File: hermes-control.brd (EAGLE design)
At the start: 106 x 47 mm, 73 parts, among them J1 1981568-1, J3 2201778-1, Q2 BC849SMD, Q3 FDN360P, Q4 FDN360P, Q5 BC849SMD, Q6 MMBT3906SOT23-3, Q7 FDN360P, Q8 MMBT2222A, U1 LSM9DS1TR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

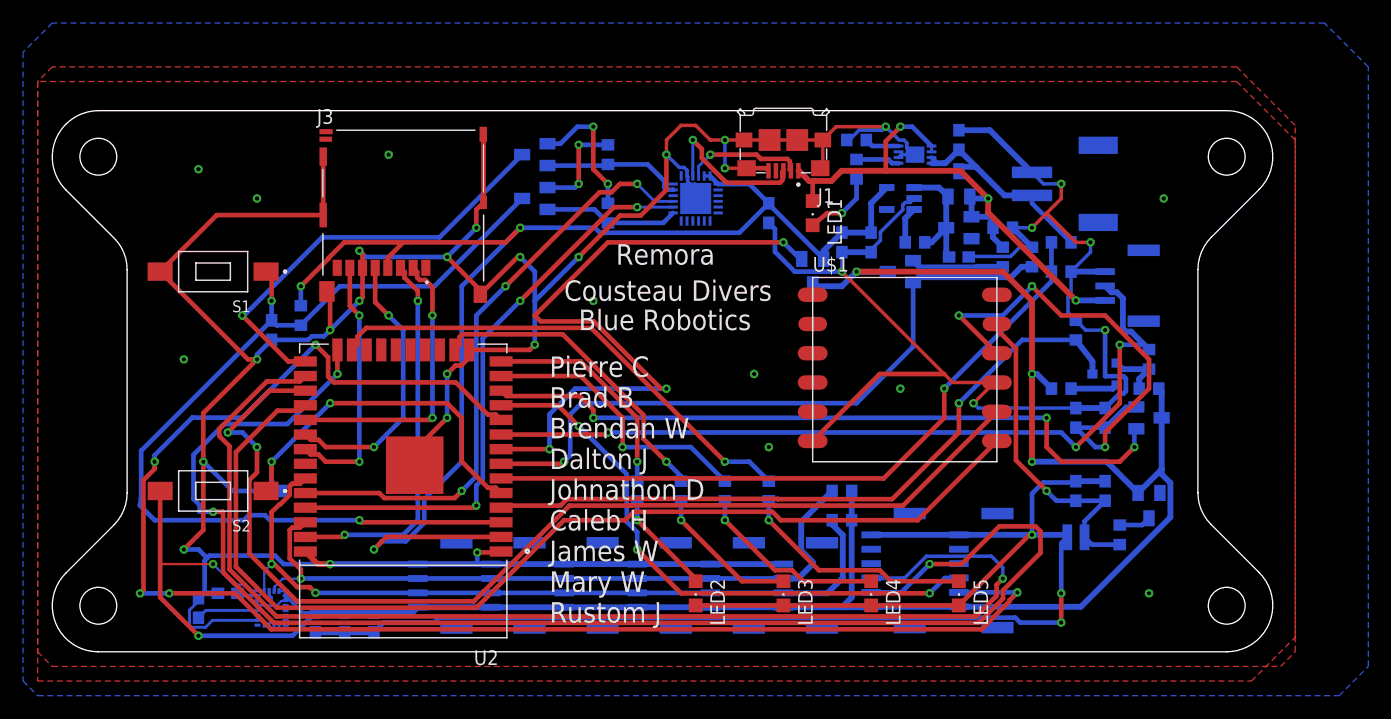
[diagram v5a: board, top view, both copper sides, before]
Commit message: adjusted vias and ground planes
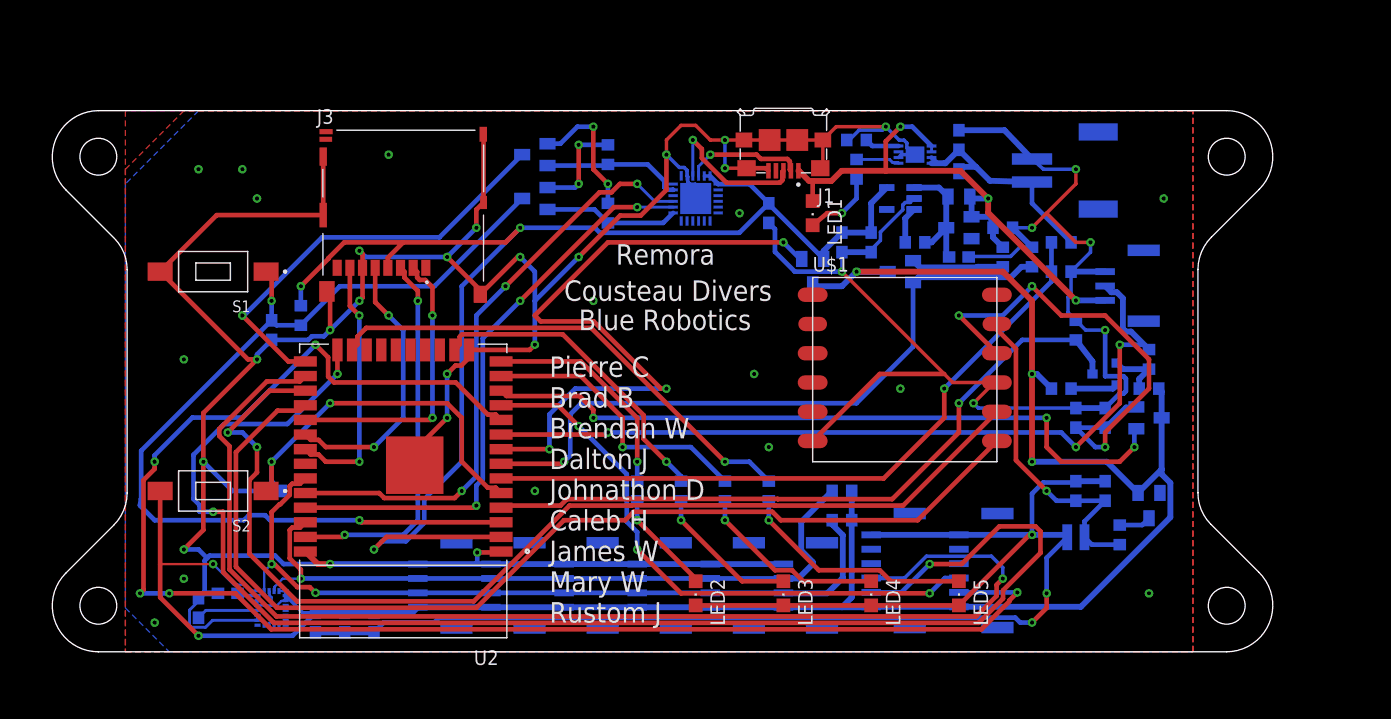
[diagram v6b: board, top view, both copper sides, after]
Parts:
- moved LBAT 1.16 mm to (85.1, 41.8)
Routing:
- net GND: track 521.6 -> 522.7 mm, vias 29 -> 43
- net V_BATT: track 19.3 -> 19.9 mm

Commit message: added test and cleaned up ground plane
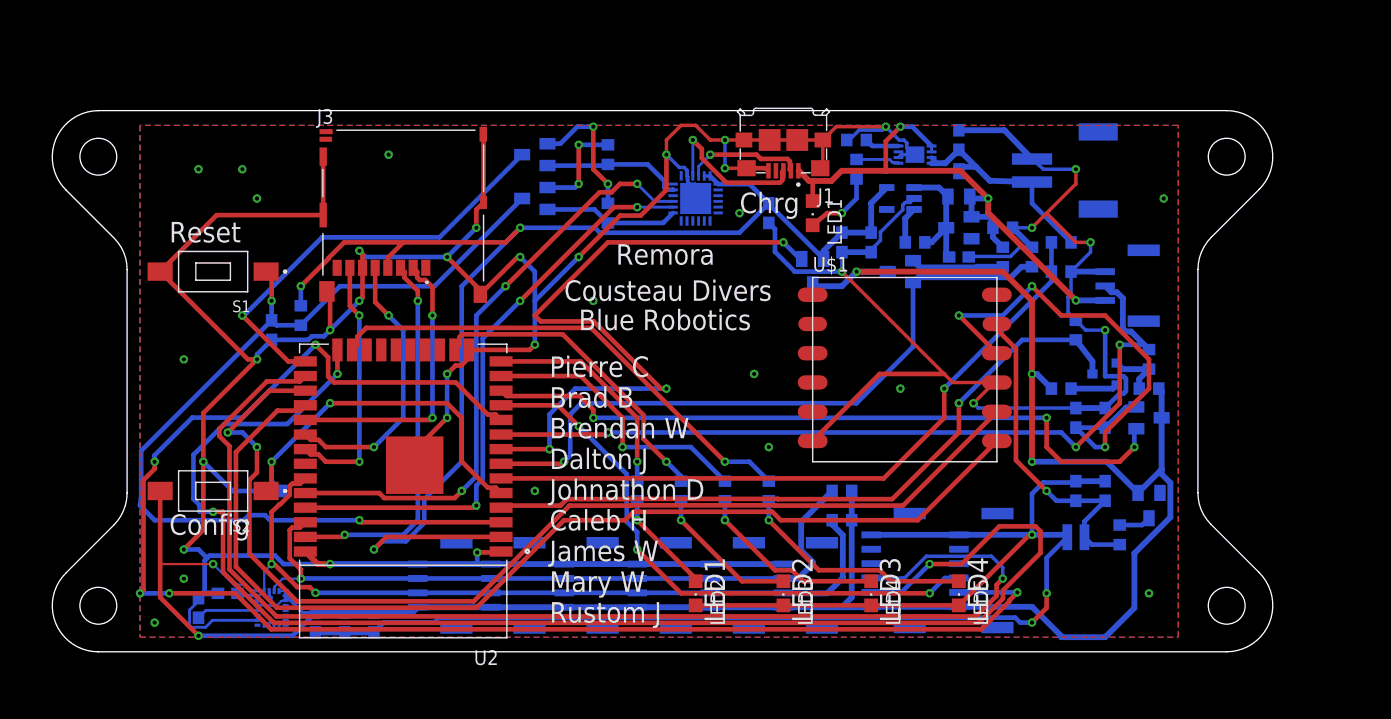
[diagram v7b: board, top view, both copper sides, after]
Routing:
- net 3.3V: track 196.0 -> 201.0 mm
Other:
- board text added: "Chrg"
- board text added: "Config"
- board text added: "LED1"
- board text added: "LED2"
- board text added: "LED3"
- board text added: "LED4"
- board text added: "Reset"
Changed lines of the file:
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@@
 <drawing>
 <settings>
-<setting alwaysvectorfont="no"/>
+<setting alwaysvectorfont="yes"/>
 <setting verticaltext="up"/>
 </settings>
-<grid distance="50" unitdist="mil" unit="mm" style="lines" multiple="1" display="yes" altdistance="5" altunitdist="mil" altunit="mm"/>
+<grid distance="50" unitdist="mil" unit="mil" style="lines" multiple="1" display="yes" altdistance="5" altunitdist="mil" altunit="mil"/>
 <layers>
 <layer number="1" name="Top" color="4" fill="1" visible="yes" active="yes"/>
@@
 <layer number="22" name="bPlace" color="7" fill="1" visible="yes" active="yes"/>
 <layer number="23" name="tOrigins" color="15" fill="1" visible="yes" active="yes"/>
-<layer number="24" name="bOrigins" color="15" fill="1" visible="yes" active="yes"/>
+<layer number="24" name="bOrigins" color="15" fill="1" visible="no" active="yes"/>
 <layer number="25" name="tNames" color="7" fill="1" visible="no" active="yes"/>
 <layer number="26" name="bNames" color="7" fill="1" visible="no" active="yes"/>
@@
 <text x="44.45" y="30.48" size="1.778" layer="21">Cousteau Divers</text>
 <text x="45.72" y="27.94" size="1.778" layer="21">Blue Robotics</text>
+<text x="10.16" y="10.16" size="1.778" layer="21">Config</text>
+<text x="10.16" y="35.56" size="1.778" layer="21">Reset</text>
+<text x="59.69" y="38.1" size="1.778" layer="21">Chrg</text>
+<text x="58.42" y="2.54" size="1.778" layer="21" rot="R90">LED1</text>
+<text x="66.04" y="2.54" size="1.778" layer="21" rot="R90">LED2</text>
+<text x="73.66" y="2.54" size="1.778" layer="21" rot="R90">LED3</text>
+<text x="81.28" y="2.54" size="1.778" layer="21" rot="R90">LED4</text>
 </plain>
 <attributes>
@@
 <wire x1="53.34" y1="40.12225" x2="53.34" y2="43.18" width="0.4064" layer="1"/>
 <polygon width="0.4064" layer="1">
-<vertex x="6.35" y="41.91"/>
-<vertex x="6.35" y="0"/>
-<vertex x="99.06" y="0"/>
-<vertex x="99.06" y="46.99"/>
-<vertex x="11.43" y="46.99"/>
-</polygon>
-<polygon width="0.4064" layer="1" isolate="0.1">
-<vertex x="6.35" y="46.99"/>
-<vertex x="6.35" y="0"/>
-<vertex x="99.06" y="0"/>
-<vertex x="99.06" y="46.99"/>
+<vertex x="7.62" y="45.72"/>
+<vertex x="7.62" y="1.27"/>
+<vertex x="97.79" y="1.27"/>
+<vertex x="97.79" y="45.72"/>
 </polygon>
 <via x="17.78" y="39.37" extent="1-16" drill="0.35"/>
 <polygon width="0.254" layer="16">
-<vertex x="6.35" y="40.64"/>
-<vertex x="6.35" y="3.81"/>
-<vertex x="10.16" y="0"/>
-<vertex x="99.06" y="0"/>
-<vertex x="99.06" y="46.99"/>
-<vertex x="12.7" y="46.99"/>
+<vertex x="7.62" y="45.72"/>
+<vertex x="7.62" y="1.27"/>
+<vertex x="97.79" y="1.27"/>
+<vertex x="97.79" y="45.72"/>
 </polygon>
 <via x="12.7" y="41.91" extent="1-16" drill="0.35"/>
@@
 <wire x1="19.05" y1="4.025" x2="19.05" y2="4.73653125" width="0.2032" layer="16"/>
 <wire x1="18.871" y1="4.91553125" x2="19.05" y2="4.73653125" width="0.2032" layer="16"/>
-<wire x1="97.1064" y1="14.6683375" x2="97.1064" y2="11.6816625" width="0.508" layer="16"/>
-<wire x1="97.1064" y1="11.6816625" x2="89.3347375" y2="3.91" width="0.508" layer="16"/>
+<wire x1="97.1064" y1="11.6816625" x2="97.1064" y2="14.6683375" width="0.508" layer="16"/>
 <wire x1="96.35" y1="15.85" x2="96.35" y2="15.4247375" width="0.508" layer="16"/>
-<wire x1="96.35" y1="15.4247375" x2="97.1064" y2="14.6683375" width="0.508" layer="16"/>
-<wire x1="89.3347375" y1="3.91" x2="78.74" y2="3.91" width="0.508" layer="16"/>
+<wire x1="97.1064" y1="14.6683375" x2="96.35" y2="15.4247375" width="0.508" layer="16"/>
 <wire x1="94.3" y1="13.8" x2="91.59" y2="16.51" width="0.508" layer="16"/>
 <wire x1="91.59" y1="16.51" x2="85.09" y2="16.51" width="0.508" layer="16"/>
@@
 <wire x1="17.2642125" y1="5.315" x2="16.7452125" y2="5.834" width="0.2032" layer="16"/>
 <wire x1="13.97" y1="7.62" x2="9.37" y2="7.62" width="0.2032" layer="1"/>
+<wire x1="78.74" y1="3.91" x2="85.09" y2="3.91" width="0.508" layer="16"/>
+<wire x1="85.09" y1="3.91" x2="87.63" y2="1.37" width="0.508" layer="16"/>
+<wire x1="87.63" y1="1.37" x2="87.63" y2="1.2715" width="0.508" layer="16"/>
+<wire x1="87.63" y1="1.2715" x2="91.44" y2="1.2715" width="0.508" layer="16"/>
+<wire x1="91.44" y1="1.2715" x2="93.98" y2="3.8115" width="0.508" layer="16"/>
+<wire x1="93.98" y1="8.5552625" x2="97.1064" y2="11.6816625" width="0.508" layer="16"/>
+<wire x1="93.98" y1="3.8115" x2="93.98" y2="8.5552625" width="0.508" layer="16"/>
 </signal>
 <signal name="N$1">

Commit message: more changes and dimension is stuck
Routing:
- net GND: track 522.7 -> 451.1 mm, vias 43 -> 46
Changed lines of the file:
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@@
 <drawing>
 <settings>
-<setting alwaysvectorfont="yes"/>
+<setting alwaysvectorfont="no"/>
 <setting verticaltext="up"/>
 </settings>
@@
 <text x="73.66" y="2.54" size="1.778" layer="21" rot="R90">LED3</text>
 <text x="81.28" y="2.54" size="1.778" layer="21" rot="R90">LED4</text>
+<dimension x1="82.55" y1="33.02" x2="69.85" y2="33.02" x3="76.2" y3="33.02" textsize="1.778" layer="1"/>
 </plain>
 <attributes>
@@
 <wire x1="85.09" y1="35.14" x2="83.4" y2="36.83" width="0.508" layer="16"/>
 <wire x1="68.58" y1="34.71" x2="71.12" y2="34.71" width="0.508" layer="16"/>
-<wire x1="27.94" y1="1.69" x2="25.4" y2="1.69" width="0.508" layer="16"/>
-<wire x1="25.4" y1="1.69" x2="22.86" y2="1.69" width="0.508" layer="16"/>
 <wire x1="13.12" y1="5.08" x2="14.39" y2="5.08" width="0.508" layer="16"/>
 <wire x1="13.12" y1="5.08" x2="12.7" y2="4.66" width="0.508" layer="16"/>
@@
 <wire x1="13.31573125" y1="2.1306" x2="13.92013125" y2="2.735" width="0.254" layer="16"/>
 <wire x1="13.92013125" y1="2.735" x2="17.83" y2="2.735" width="0.254" layer="16"/>
-<wire x1="27.94" y1="1.69" x2="28.79" y2="2.54" width="0.4064" layer="16"/>
-<via x="85.09" y="2.54" extent="1-16" drill="0.35"/>
-<wire x1="28.79" y1="2.54" x2="33.16710625" y2="2.54" width="0.4064" layer="16"/>
-<wire x1="84.06289375" y1="2.54" x2="85.09" y2="2.54" width="0.4064" layer="16"/>
-<wire x1="83.63729375" y1="2.9656" x2="84.06289375" y2="2.54" width="0.4064" layer="16"/>
-<wire x1="33.16710625" y1="2.54" x2="33.59270625" y2="2.9656" width="0.4064" layer="16"/>
-<wire x1="33.59270625" y1="2.9656" x2="83.63729375" y2="2.9656" width="0.4064" layer="16"/>
-<wire x1="86.36" y1="5.08" x2="86.36" y2="3.81" width="0.4064" layer="1"/>
-<wire x1="85.09" y1="2.54" x2="86.36" y2="3.81" width="0.4064" layer="1"/>
-<via x="86.36" y="5.08" extent="1-16" drill="0.35"/>
-<wire x1="86.36" y1="5.08" x2="86.36" y2="8.16" width="0.4064" layer="16"/>
-<wire x1="86.36" y1="8.16" x2="88.15" y2="9.95" width="0.4064" layer="16"/>
 <wire x1="13.66605" y1="8.3538" x2="13.451125" y2="8.138875" width="0.4064" layer="16"/>
 <wire x1="13.451125" y1="8.138875" x2="13.2362" y2="7.92395" width="0.4064" layer="16"/>
@@
 <wire x1="51.10395" y1="37.8862" x2="53.34" y2="40.12225" width="0.4064" layer="1"/>
 <wire x1="53.34" y1="40.12225" x2="53.34" y2="43.18" width="0.4064" layer="1"/>
-<polygon width="0.4064" layer="1">
+<polygon width="0.4064" layer="1" spacing="0.1" isolate="0.002540625">
 <vertex x="7.62" y="45.72"/>
 <vertex x="7.62" y="1.27"/>
@@
 <via x="41.91" y="13.97" extent="1-16" drill="0.35"/>
 <via x="59.69" y="38.1" extent="1-16" drill="0.35"/>
+<via x="41.91" y="20.32" extent="1-16" drill="0.35"/>
+<via x="41.91" y="11.43" extent="1-16" drill="0.35"/>
+<via x="57.15" y="10.16" extent="1-16" drill="0.35"/>
+<via x="63.5" y="8.89" extent="1-16" drill="0.35"/>
+<via x="19.05" y="21.59" extent="1-16" drill="0.35"/>
+<wire x1="17.83" y1="2.735" x2="22.86" y2="1.69" width="0" layer="19" extent="16-16"/>
 </signal>
 <signal name="3.3V">
@@
 <wire x1="24.765" y1="26.22" x2="24.765" y2="24.13" width="0.4064" layer="1"/>
 <via x="24.765" y="24.13" extent="1-16" drill="0.35"/>
-<wire x1="12.7988" y1="12.1638" x2="13.97" y2="12.1638" width="0.4064" layer="16"/>
 <via x="13.97" y="12.1638" extent="1-16" drill="0.35"/>
-<wire x1="12.2644" y1="13.27270625" x2="12.7988" y2="12.73830625" width="0.4064" layer="16"/>
-<wire x1="12.7988" y1="12.73830625" x2="12.7988" y2="12.1638" width="0.4064" layer="16"/>
 <wire x1="24.765" y1="24.13" x2="20.4188" y2="19.7838" width="0.4064" layer="16"/>
 <wire x1="20.4188" y1="19.7838" x2="14.93605" y2="19.7838" width="0.4064" layer="16"/>
@@
 <wire x1="82.24605" y1="10.8938" x2="78.97225" y2="7.62" width="0.4064" layer="1"/>
 <wire x1="78.97225" y1="7.62" x2="76.2" y2="7.62" width="0.4064" layer="1"/>
+<wire x1="12.2644" y1="13.27270625" x2="13.37330625" y2="12.1638" width="0.4064" layer="16"/>
+<wire x1="13.37330625" y1="12.1638" x2="13.97" y2="12.1638" width="0.4064" layer="16"/>
 </signal>
 <signal name="RX2">
@@
 <wire x1="26.85" y1="11.25" x2="26.67" y2="11.43" width="0.4064" layer="1"/>
 <via x="26.67" y="11.43" extent="1-16" drill="0.35"/>
-<wire x1="8.89" y1="11.43" x2="7.62" y2="12.7" width="0.4064" layer="16"/>
 <wire x1="18.47729375" y1="11.8656" x2="17.08270625" y2="11.8656" width="0.4064" layer="16"/>
 <wire x1="26.67" y1="11.43" x2="18.91289375" y2="11.43" width="0.4064" layer="16"/>
@@
 <wire x1="18.91289375" y1="11.43" x2="18.47729375" y2="11.8656" width="0.4064" layer="16"/>
 <wire x1="17.08270625" y1="11.8656" x2="16.64710625" y2="11.43" width="0.4064" layer="16"/>
-<wire x1="7.62" y1="12.7" x2="7.62" y2="12.77128125" width="0.4064" layer="16"/>
-<wire x1="7.62" y1="12.77128125" x2="7.70100625" y2="13.2770875" width="0.4064" layer="16"/>
 <wire x1="7.72056875" y1="17.46056875" x2="19.05" y2="28.79" width="0.4064" layer="16"/>
 <wire x1="7.70100625" y1="13.2770875" x2="7.72056875" y2="13.29665" width="0.4064" layer="16"/>
 <wire x1="7.72056875" y1="13.29665" x2="7.72056875" y2="17.46056875" width="0.4064" layer="16"/>
+<wire x1="8.89" y1="11.43" x2="7.72056875" y2="12.59943125" width="0.4064" layer="16"/>
+<wire x1="7.72056875" y1="12.59943125" x2="7.72056875" y2="13.29665" width="0.4064" layer="16"/>
 </signal>
 <signal name="N$19">
